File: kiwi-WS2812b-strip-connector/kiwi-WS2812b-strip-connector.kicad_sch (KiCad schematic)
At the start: 12 parts, among them J1 Conn_01x03, J2 Conn_01x03, SW1 SW_Push, U2 WS2812B_fromStrip, U4 WS2812B_fromStrip, U5 WS2812B_toStrip, U7 WS2812B_toStrip

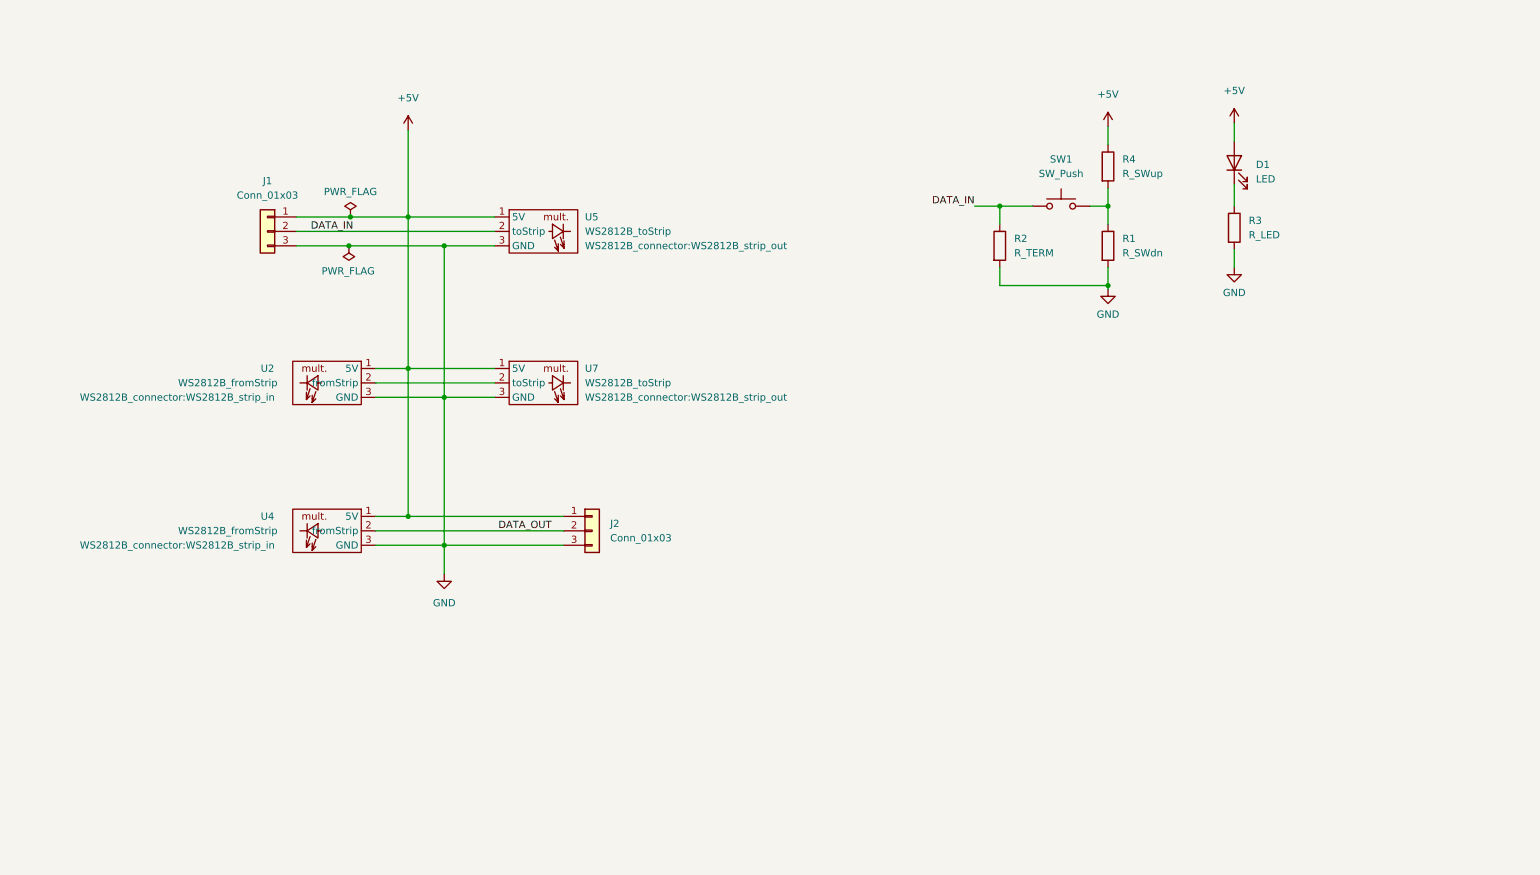
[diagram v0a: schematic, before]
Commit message: Added USB connector as alternate footprint
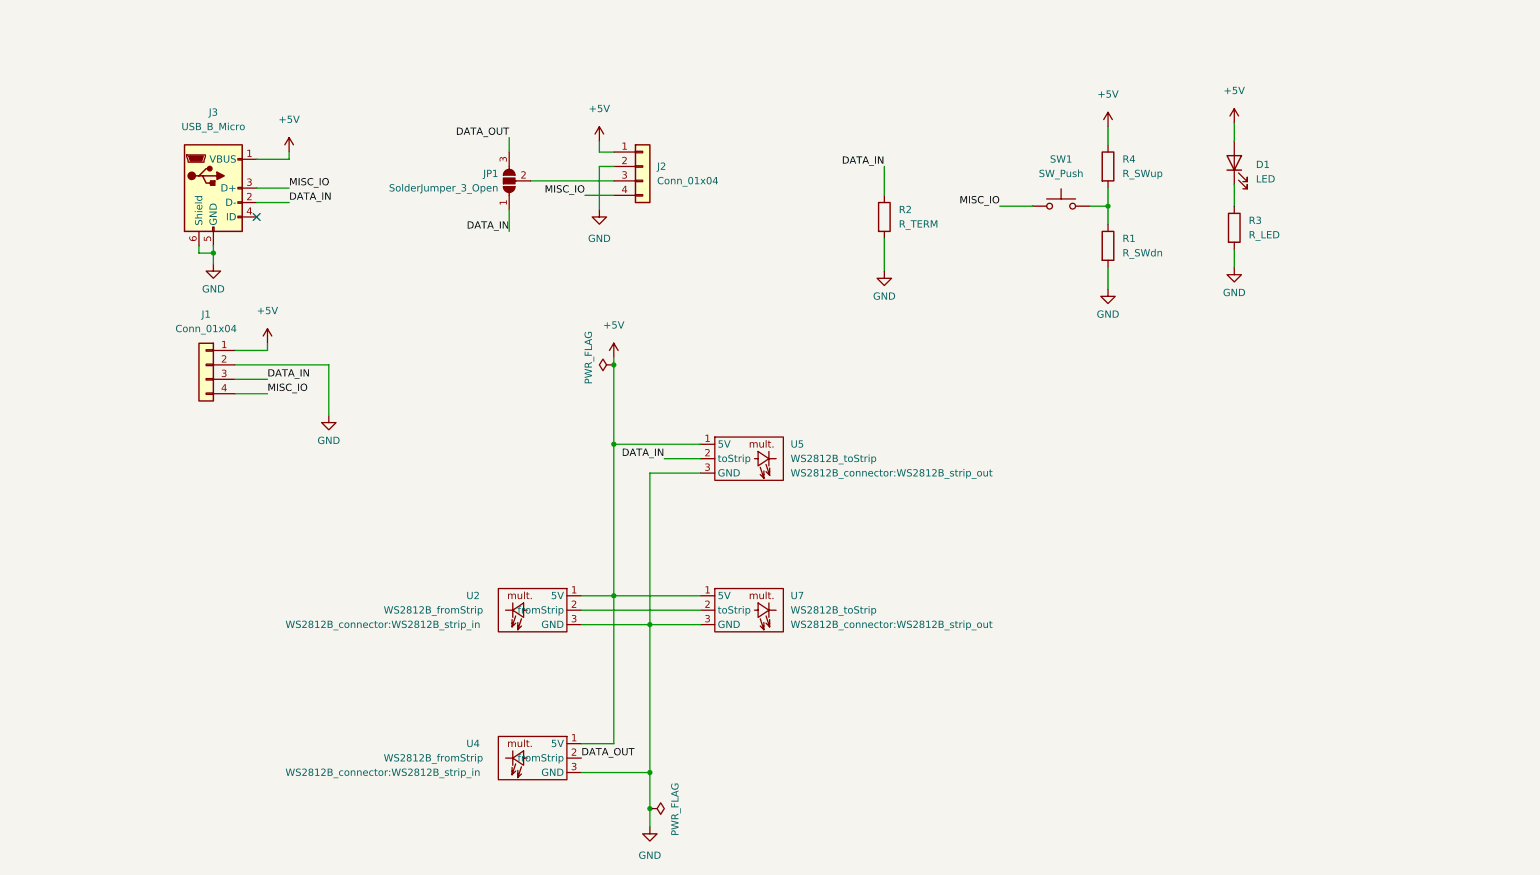
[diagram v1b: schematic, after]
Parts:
- removed J1, J2: Conn_01x03, Connector_JST:JST_PH_S3B-PH-K_1x03_P2.00mm_Horizontal, symbol Connector_Generic:Conn_01x03
- added J1, J2: Conn_01x04, Connector_JST:JST_PH_S4B-PH-K_1x04_P2.00mm_Horizontal, symbol Connector_Generic:Conn_01x04
- added J3: USB_B_Micro, Connector_USB_Extra:USB_Micro_MIUSB-F5M-BB-U, symbol Connector:USB_B_Micro
- added JP1: SolderJumper_3_Open, Jumper:SolderJumper-3_P2.0mm_Open_TrianglePad1.0x1.5mm, symbol Jumper:SolderJumper_3_Open
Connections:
- net +5V: now also J1.1 (Pin_1), J2.1 (Pin_1), J3.1 (VBUS)
- net DATA_IN: now also J1.3 (Pin_3), J3.2 (D-), JP1.1 (A); no longer SW1.1
- net DATA_OUT: now also JP1.3 (B)
- net GND: now also J1.2 (Pin_2), J2.2 (Pin_2), J3.5 (GND), J3.6 (Shield)
- new net: J2.3 (Pin_3), JP1.2 (C)
- new net MISC_IO: J1.4 (Pin_4), J2.4 (Pin_4), J3.3 (D+), SW1.1
- no-connect marks 0 -> 1
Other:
- moved on the sheet: R2, U2, U4, U5, U7

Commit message: Commented schematics and updated PCB, both pass DRC
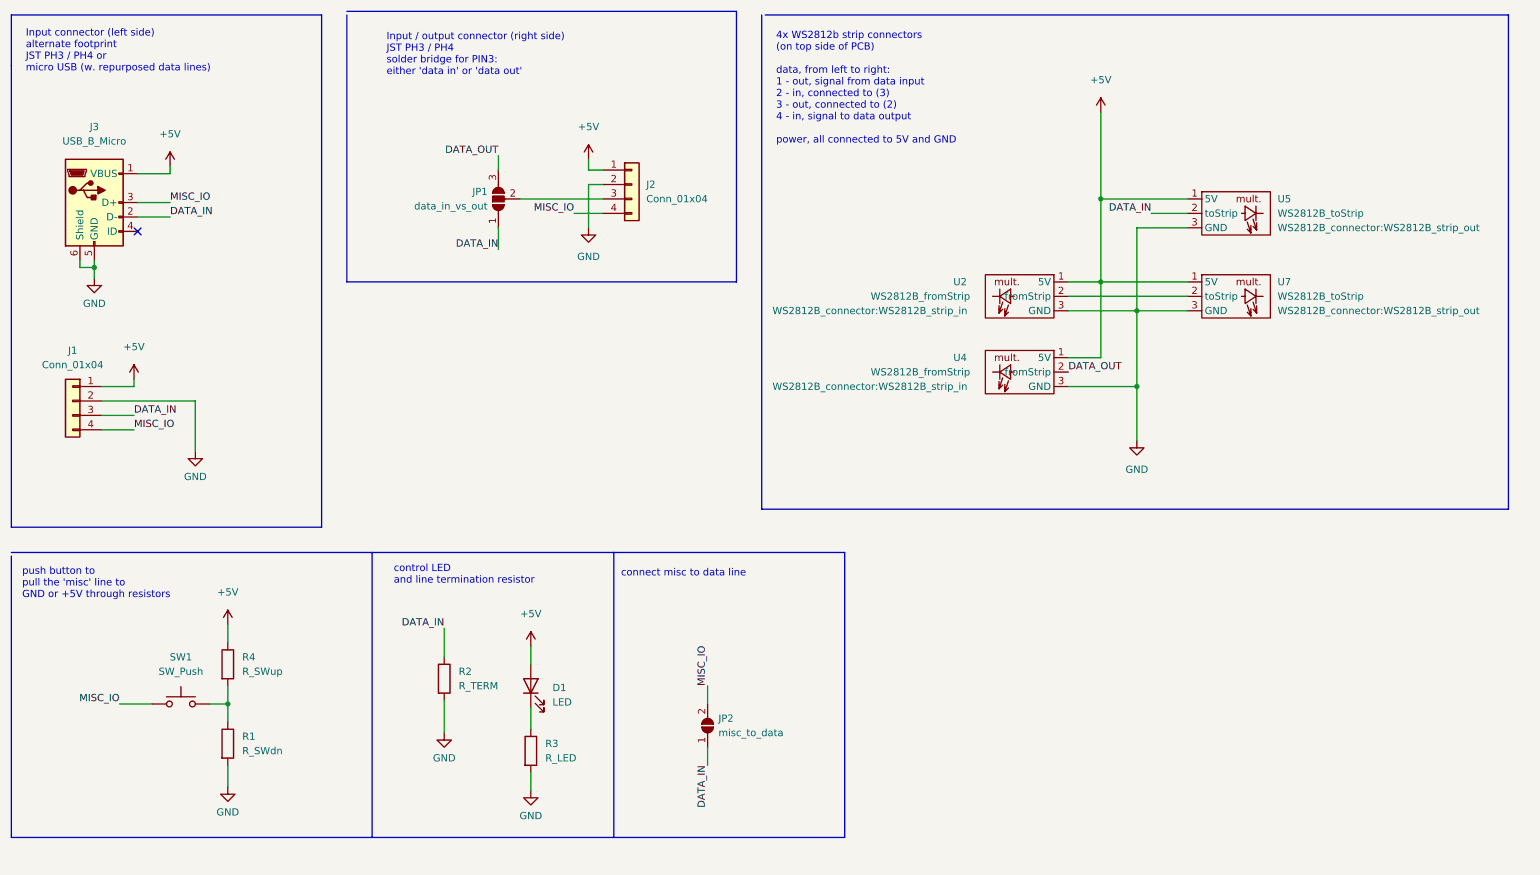
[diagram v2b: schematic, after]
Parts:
- added JP2: misc_to_data, Jumper:SolderJumper-2_P1.3mm_Open_RoundedPad1.0x1.5mm, symbol Jumper:SolderJumper_2_Open
- JP1: value SolderJumper_3_Open -> data_in_vs_out; footprint Jumper:SolderJumper-3_P2.0mm_Open_TrianglePad1.0x1.5mm -> Jumper:SolderJumper-3_P1.3mm_Open_RoundedPad1.0x1.5mm
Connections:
- net DATA_IN: now also JP2.1 (A)
- net MISC_IO: now also JP2.2 (B)
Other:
- note added: "4x WS2812b strip connectors (on top side of PCB) data, from left to right: 1 - out, signal from data input 2 - in, connected to (3) 3 - out, connected to (2) 4 - in, signal to data output power, all connected to 5V and GND"
- note added: "Input / output connector (right side) JST PH3 / PH4 solder bridge for PIN3: either 'data in' or 'data out'"
- note added: "Input connector (left side) alternate footprint JST PH3 / PH4 or micro USB (w. repurposed data lines)"
- note added: "connect misc to data line"
- note added: "control LED and line termination resistor"
- note added: "push button to pull the 'misc' line to GND or +5V through resistors"
- moved on the sheet: D1, J1, J2, J3, JP1, R1, R2, R3, R4, SW1, U2, U4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
